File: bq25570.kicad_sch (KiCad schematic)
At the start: 27 parts, among them J6 Conn_01x03_Pin, U3 BQ25570, U5 TPS2116DRL

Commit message: footprint assignment
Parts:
- CIN1, COUT1, CSTOR1: footprint Capacitor_SMD:C_0402_1005Metric_Pad0.74x0.62mm_HandSolder -> Capacitor_SMD:C_0603_1608Metric_Pad1.08x0.95mm_HandSolder
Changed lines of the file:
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@@
 	)
 	(junction
-		(at 186.69 72.39)
-		(diameter 0)
-		(color 0 0 0 0)
-	)
-	(junction
 		(at 83.185 90.17)
 		(diameter 0)
@@
 	(wire
 		(pts
-			(xy 175.895 72.39) (xy 186.69 72.39)
+			(xy 175.895 72.39) (xy 198.755 72.39)
 		)
 		(stroke
@@
 	(wire
 		(pts
-			(xy 186.69 72.39) (xy 198.755 72.39)
-		)
-		(stroke
-			(width 0)
-			(type default)
-		)
-	)
-	(wire
-		(pts
 			(xy 69.215 73.66) (xy 69.215 81.28)
 		)
@@
 	)
 	(symbol
-		(lib_id "power:PWR_FLAG")
-		(at 186.69 72.39 0)
-		(unit 1)
-		(exclude_from_sim no)
-		(in_bom yes)
-		(on_board yes)
-		(dnp no)
-		(fields_autoplaced yes)
-		(property "Reference" "#FLG03"
-			(at 186.69 70.485 0)
-			(effects
-				(font
-					(size 1.27 1.27)
-				)
-				(hide yes)
-			)
-		)
-		(property "Value" "PWR_FLAG"
-			(at 186.69 67.31 0)
-			(effects
-				(font
-					(size 1.27 1.27)
-				)
-			)
-		)
-		(property "Footprint" ""
-			(at 186.69 72.39 0)
-			(effects
-				(font
-					(size 1.27 1.27)
-				)
-				(hide yes)
-			)
-		)
-		(property "Datasheet" "~"
-			(at 186.69 72.39 0)
-			(effects
-				(font
-					(size 1.27 1.27)
-				)
-				(hide yes)
-			)
-		)
-		(property "Description" "Special symbol for telling ERC where power comes from"
-			(at 186.69 72.39 0)
-			(effects
-				(font
-					(size 1.27 1.27)
-				)
-				(hide yes)
-			)
-		)
-		(pin "1"
-		)
-		(instances
-			(project "lora-stmu535-lr1121-tx"
-				(path "/963238c7-8564-44c5-a128-5d82375c10f7/ec0d794e-4e86-49b4-99a7-5aeb461302ab"
-					(reference "#FLG03")
-					(unit 1)
-				)
-			)
-		)
-	)
-	(symbol
 		(lib_id "Battery_Management:BQ25570")
 		(at 145.415 86.36 0)
@@
 			)
 		)
-		(property "Footprint" "Capacitor_SMD:C_0402_1005Metric_Pad0.74x0.62mm_HandSolder"
+		(property "Footprint" "Capacitor_SMD:C_0603_1608Metric_Pad1.08x0.95mm_HandSolder"
 			(at 107.95 80.645 0)
 			(effects
@@
 			)
 		)
-		(property "Footprint" "Capacitor_SMD:C_0402_1005Metric_Pad0.74x0.62mm_HandSolder"
+		(property "Footprint" "Capacitor_SMD:C_0603_1608Metric_Pad1.08x0.95mm_HandSolder"
 			(at 181.61 78.74 0)
 			(effects
@@
 			)
 		)
-		(property "Footprint" "Capacitor_SMD:C_0402_1005Metric_Pad0.74x0.62mm_HandSolder"
+		(property "Footprint" "Capacitor_SMD:C_0603_1608Metric_Pad1.08x0.95mm_HandSolder"
 			(at 132.715 51.435 0)
 			(effects

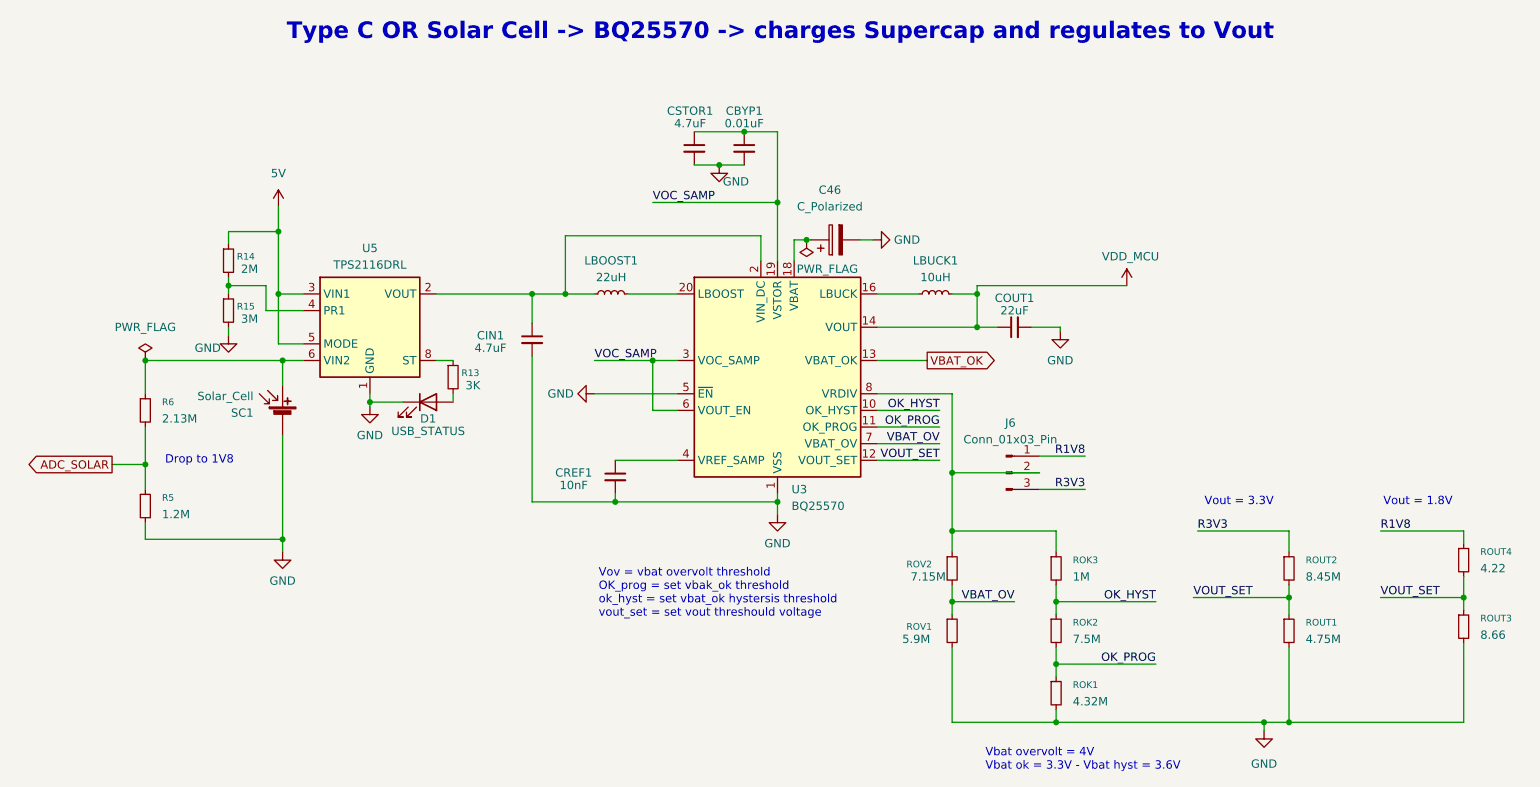
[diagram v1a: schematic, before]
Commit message: separated matching lines
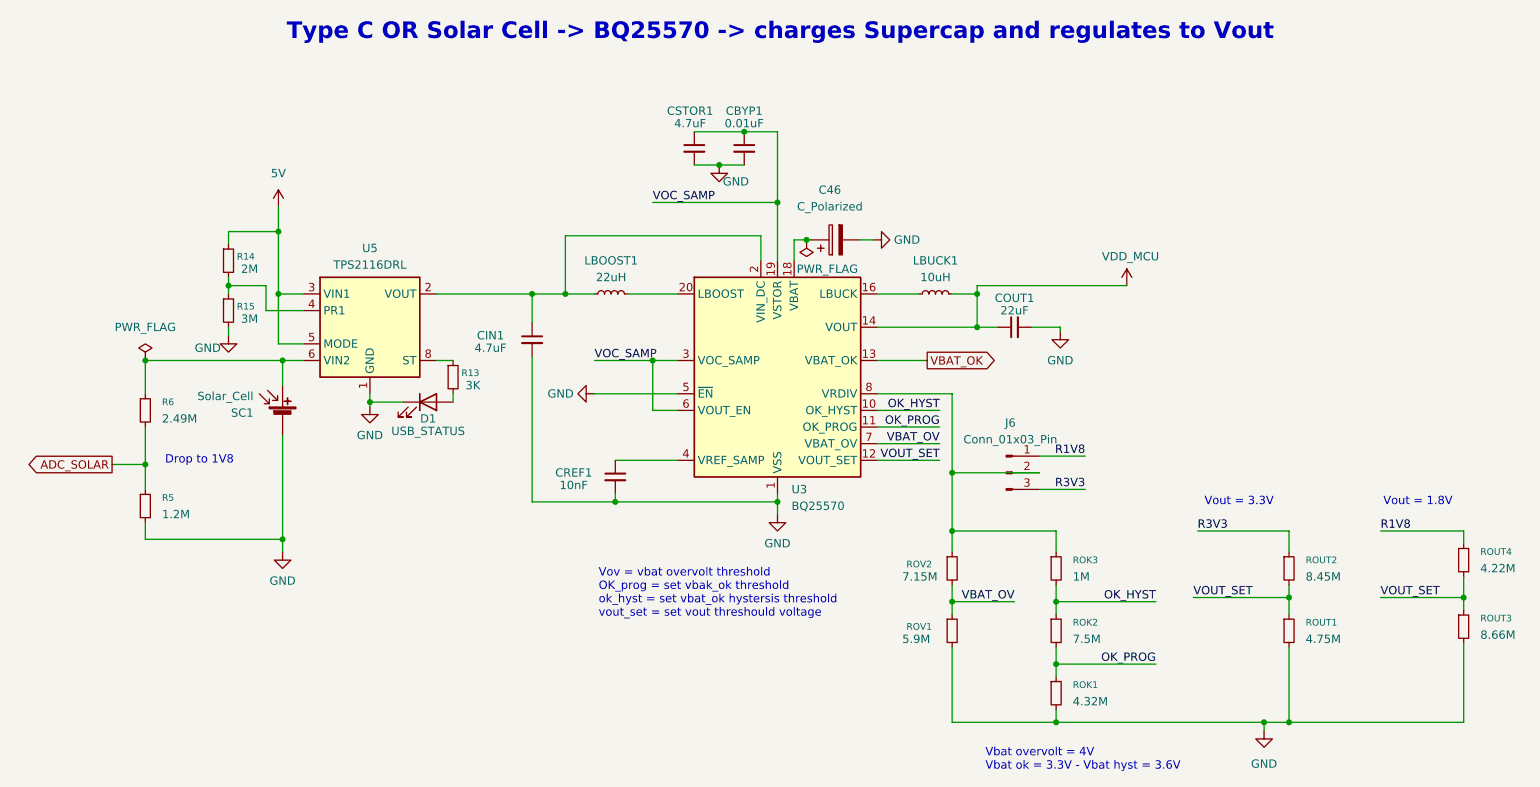
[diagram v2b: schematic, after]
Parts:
- LBUCK1: footprint Inductor_SMD:L_0402_1005Metric_Pad0.77x0.64mm_HandSolder -> Inductor_SMD:L_0603_1608Metric_Pad1.05x0.95mm_HandSolder
- R6: value 2.13M -> 2.49M
- ROUT3: value 8.66 -> 8.66M
- ROUT4: value 4.22 -> 4.22M
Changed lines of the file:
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@@
 		)
 		(property "Value" "7.15M"
-			(at 165.735 116.84 0)
+			(at 164.465 116.84 0)
 			(effects
 				(font
@@
 			)
 		)
-		(property "Value" "8.66"
+		(property "Value" "8.66M"
 			(at 252.73 125.7299 0)
 			(effects
@@
 			)
 		)
-		(property "Value" "4.22"
+		(property "Value" "4.22M"
 			(at 252.73 115.5699 0)
 			(effects
@@
 			)
 		)
-		(property "Value" "2.13M"
+		(property "Value" "2.49M"
 			(at 51.435 92.7099 0)
 			(effects
@@
 			)
 		)
-		(property "Footprint" "Inductor_SMD:L_0402_1005Metric_Pad0.77x0.64mm_HandSolder"
+		(property "Footprint" "Inductor_SMD:L_0603_1608Metric_Pad1.05x0.95mm_HandSolder"
 			(at 169.545 73.66 0)
 			(effects
